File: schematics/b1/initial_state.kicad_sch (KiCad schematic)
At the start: 18 parts, among them SW1 SW_SPDT, SW2 SW_SPDT, SW3 SW_SPDT, SW4 SW_SPDT, SW5 SW_SPDT, SW6 SW_SPDT, SW7 SW_SPDT, SW8 SW_Push, U1 74HC165

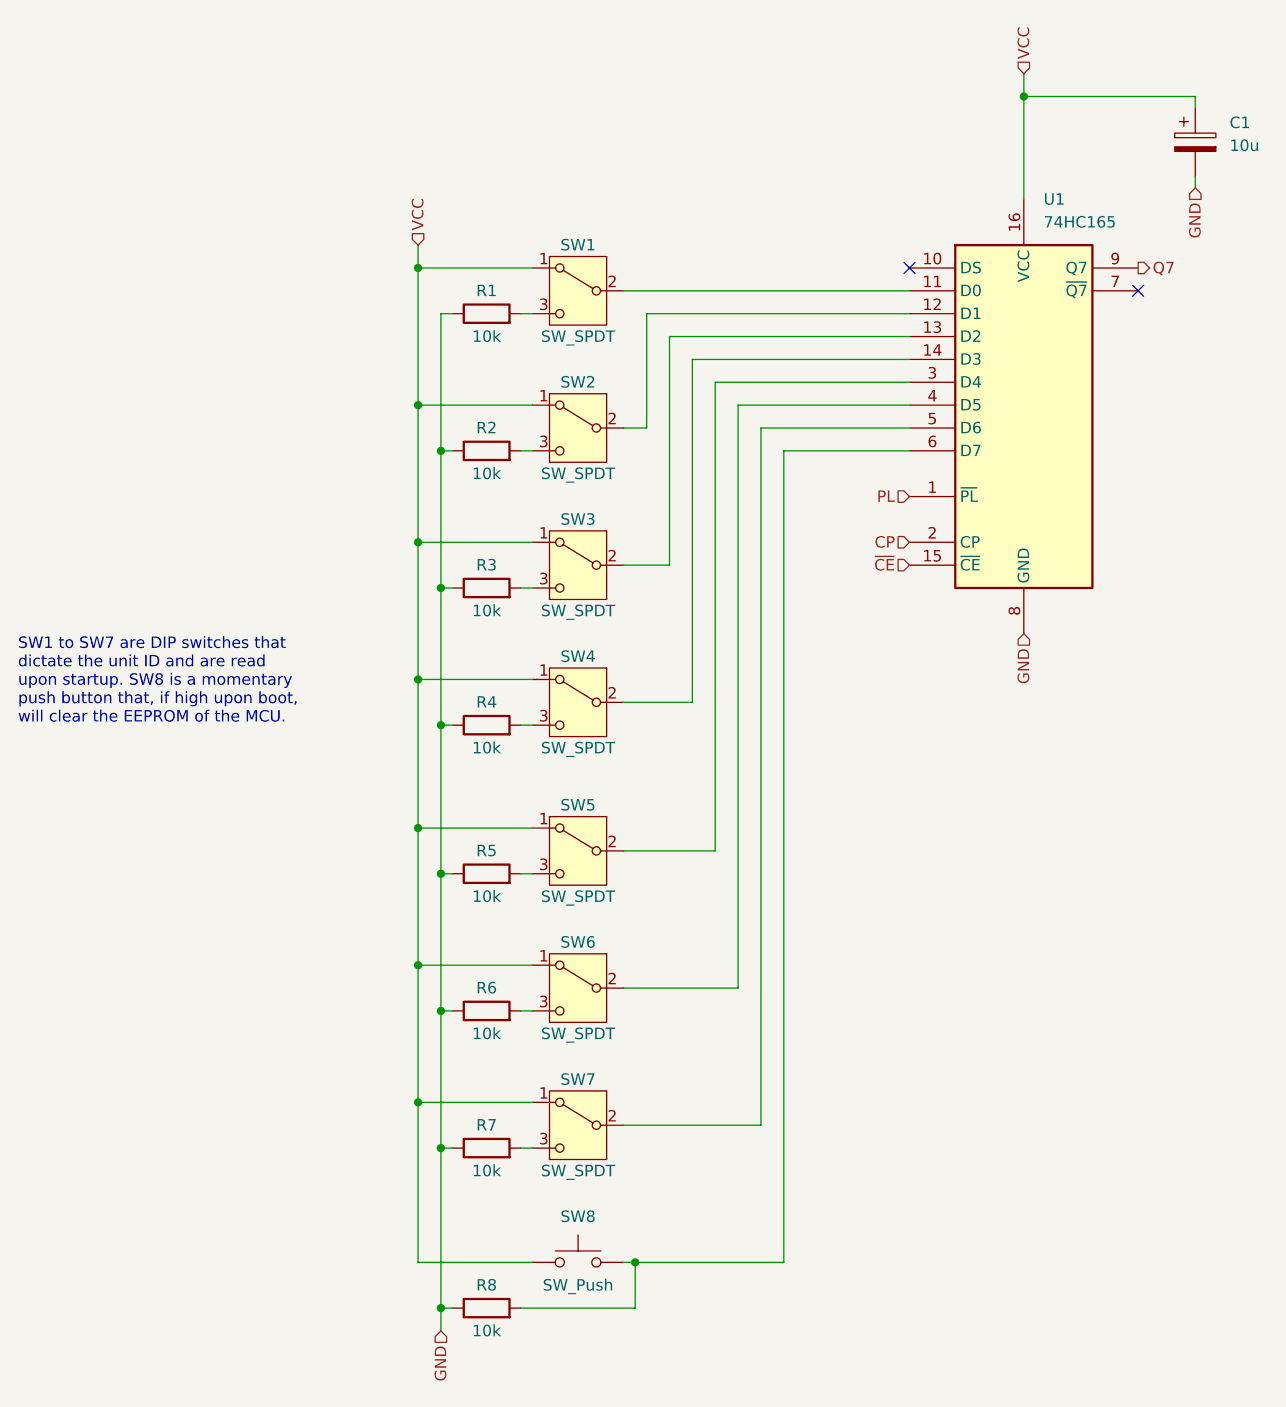
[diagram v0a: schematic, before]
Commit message: Changed GND hierarchical labels to global.
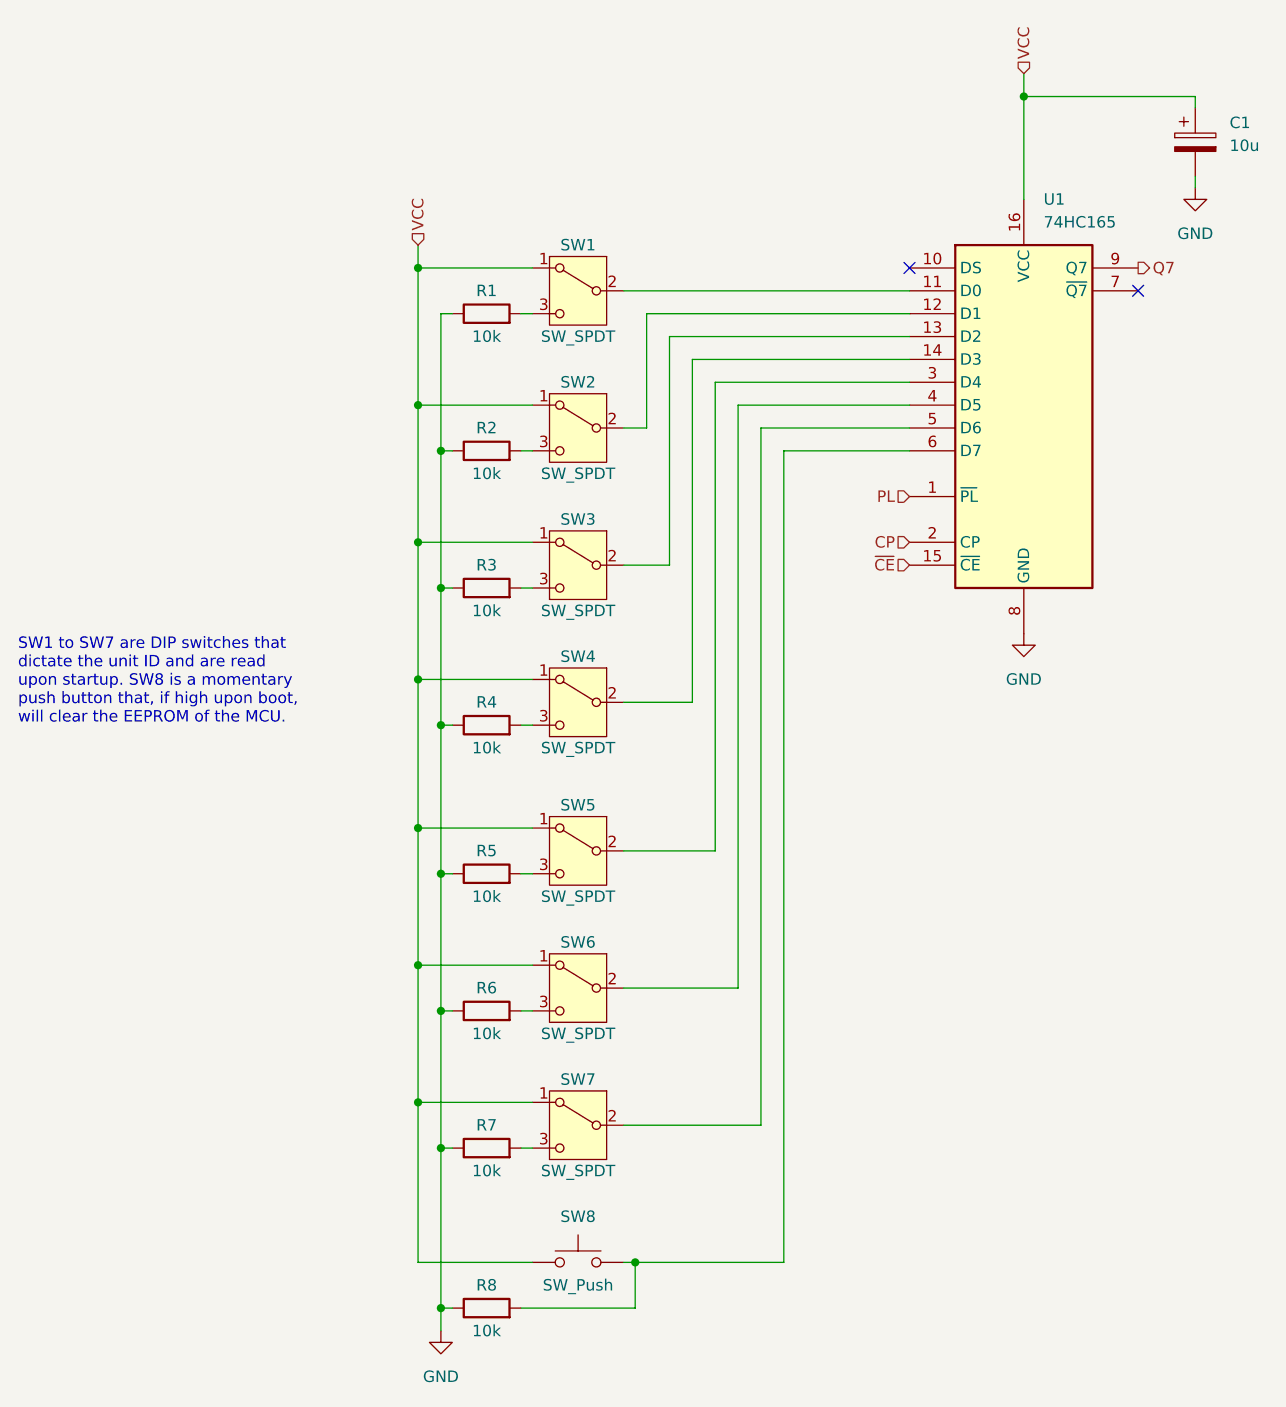
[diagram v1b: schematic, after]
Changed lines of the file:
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@@
     (effects (font (size 1.27 1.27)) (justify left bottom))
-  )
-  (hierarchical_label "GND" (shape input) (at 170.18 93.98 270) (fields_autoplaced)
-    (effects (font (size 1.27 1.27)) (justify right))
   )
   (hierarchical_label "PL" (shape input) (at 157.48 78.74 180) (fields_autoplaced)
     (effects (font (size 1.27 1.27)) (justify right))
   )
-  (hierarchical_label "GND" (shape input) (at 189.23 44.45 270) (fields_autoplaced)
-    (effects (font (size 1.27 1.27)) (justify right))
-  )
   (hierarchical_label "VCC" (shape input) (at 170.18 31.75 90) (fields_autoplaced)
     (effects (font (size 1.27 1.27)) (justify left))
   )
+  (hierarchical_label "VCC" (shape input) (at 102.87 50.8 90) (fields_autoplaced)
+    (effects (font (size 1.27 1.27)) (justify left))
+  )
   (hierarchical_label "~{CE}" (shape input) (at 157.48 86.36 180) (fields_autoplaced)
     (effects (font (size 1.27 1.27)) (justify right))
   )
-  (hierarchical_label "GND" (shape input) (at 105.41 171.45 270) (fields_autoplaced)
-    (effects (font (size 1.27 1.27)) (justify right))
-  )
   (hierarchical_label "CP" (shape input) (at 157.48 83.82 180) (fields_autoplaced)
     (effects (font (size 1.27 1.27)) (justify right))
@@
     (effects (font (size 1.27 1.27)) (justify left))
   )
-  (hierarchical_label "VCC" (shape input) (at 102.87 50.8 90) (fields_autoplaced)
-    (effects (font (size 1.27 1.27)) (justify left))
+  (symbol (lib_id "power:GND") (at 170.18 93.98 0) (unit 1)
+    (in_bom yes) (on_board yes) (dnp no) (fields_autoplaced)
+    (property "Reference" "#PWR04" (at 170.18 100.33 0)
+      (effects (font (size 1.27 1.27)) hide)
+    )
+    (property "Value" "GND" (at 170.18 99.06 0)
+      (effects (font (size 1.27 1.27)))
+    )
+    (property "Footprint" "" (at 170.18 93.98 0)
+      (effects (font (size 1.27 1.27)) hide)
+    )
+    (property "Datasheet" "" (at 170.18 93.98 0)
+      (effects (font (size 1.27 1.27)) hide)
+    )
+    (pin "1")
+    (instances
+      (project "b1"
+        (path "/d6142fa5-2354-4512-9919-37616259c364/15951702-f191-4c4b-b68c-efdb5de618b5"
+          (reference "#PWR04") (unit 1)
+        )
+      )
+    )
   )
   (symbol (lib_id "Switch:SW_SPDT") (at 120.65 148.59 0) (mirror y) (unit 1)
@@
     )
   )
+  (symbol (lib_id "power:GND") (at 105.41 171.45 0) (unit 1)
+    (in_bom yes) (on_board yes) (dnp no) (fields_autoplaced)
+    (property "Reference" "#PWR03" (at 105.41 177.8 0)
+      (effects (font (size 1.27 1.27)) hide)
+    )
+    (property "Value" "GND" (at 105.41 176.53 0)
+      (effects (font (size 1.27 1.27)))
+    )
+    (property "Footprint" "" (at 105.41 171.45 0)
+      (effects (font (size 1.27 1.27)) hide)
+    )
+    (property "Datasheet" "" (at 105.41 171.45 0)
+      (effects (font (size 1.27 1.27)) hide)
+    )
+    (pin "1")
+    (instances
+      (project "b1"
+        (path "/d6142fa5-2354-4512-9919-37616259c364/15951702-f191-4c4b-b68c-efdb5de618b5"
+          (reference "#PWR03") (unit 1)
+        )
+      )
+    )
+  )
   (symbol (lib_id "Switch:SW_SPDT") (at 120.65 55.88 0) (mirror y) (unit 1)
     (in_bom yes) (on_board yes) (dnp no)
@@
         )
       )
+    )
+  )
+  (symbol (lib_id "power:GND") (at 189.23 44.45 0) (unit 1)
+    (in_bom yes) (on_board yes) (dnp no) (fields_autoplaced)
+    (property "Reference" "#PWR05" (at 189.23 50.8 0)
+      (effects (font (size 1.27 1.27)) hide)
+    )
+    (property "Value" "GND" (at 189.23 49.53 0)
+      (effects (font (size 1.27 1.27)))
+    )
+    (property "Footprint" "" (at 189.23 44.45 0)
+      (effects (font (size 1.27 1.27)) hide)
+    )
+    (property "Datasheet" "" (at 189.23 44.45 0)
+      (effects (font (size 1.27 1.27)) hide)
+    )
+    (pin "1")
+    (instances
+      (project "b1"
+        (path "/d6142fa5-2354-4512-9919-37616259c364/15951702-f191-4c4b-b68c-efdb5de618b5"
+          (reference "#PWR05") (unit 1)
+        )
+      )
